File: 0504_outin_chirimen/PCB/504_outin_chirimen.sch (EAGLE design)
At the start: 34 parts

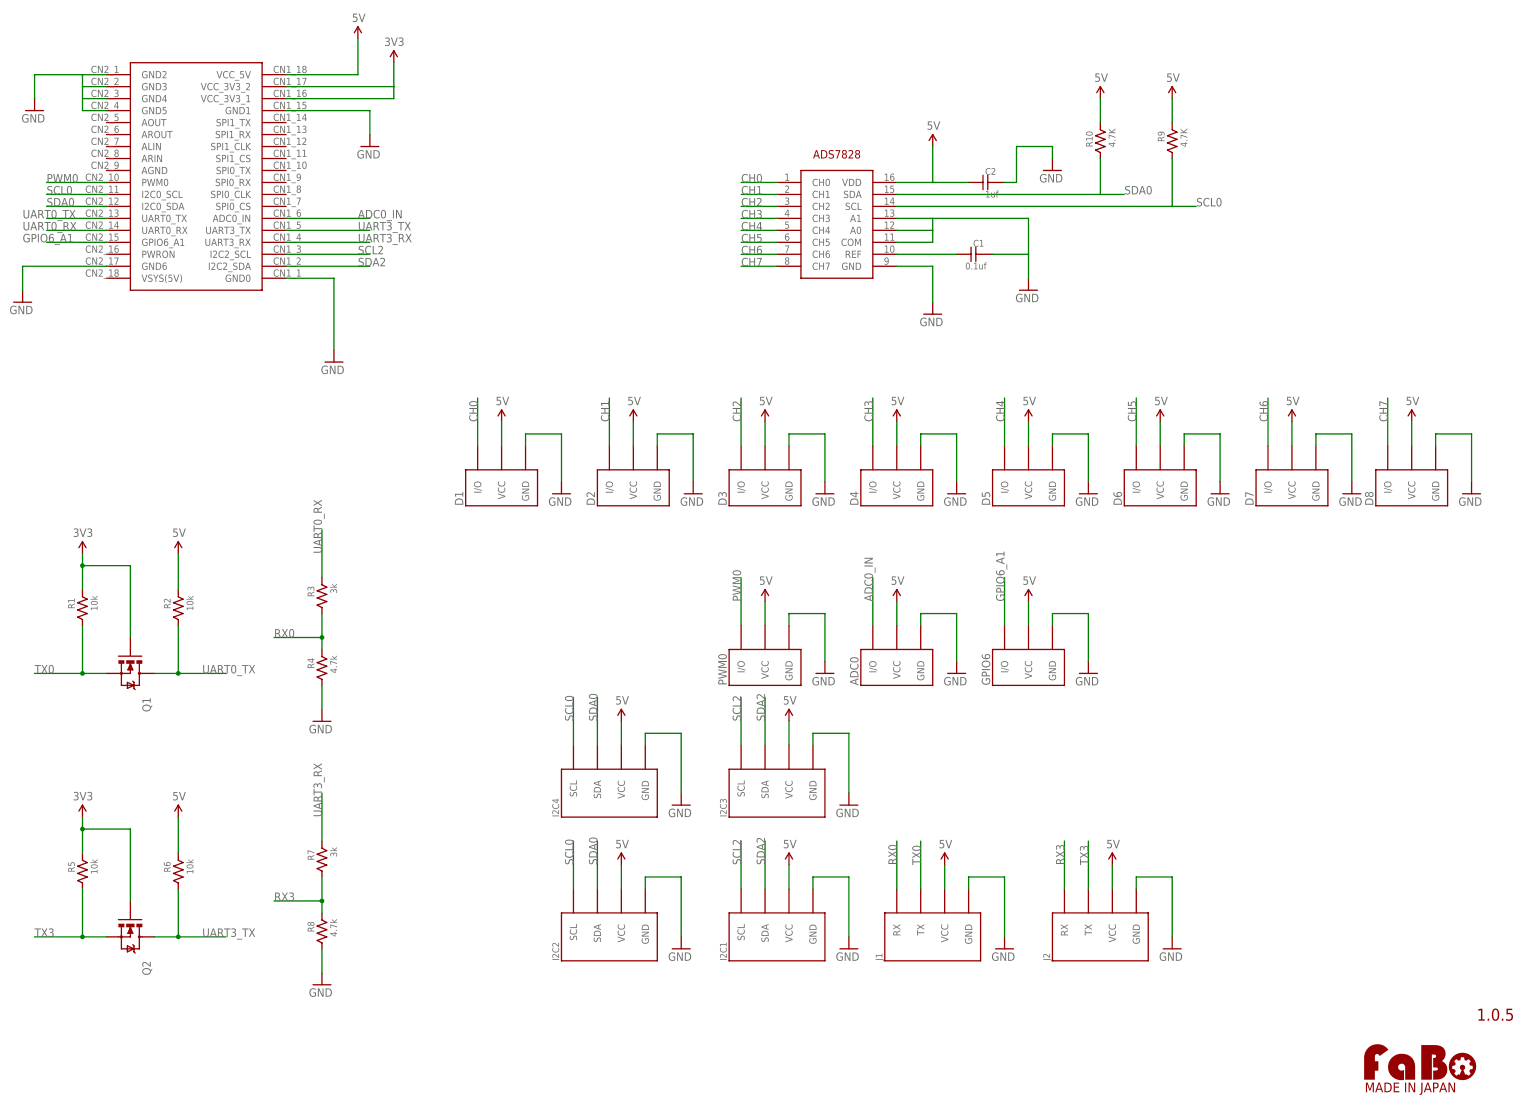
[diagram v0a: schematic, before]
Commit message: #504 outin_chirimen　ロゴ修正
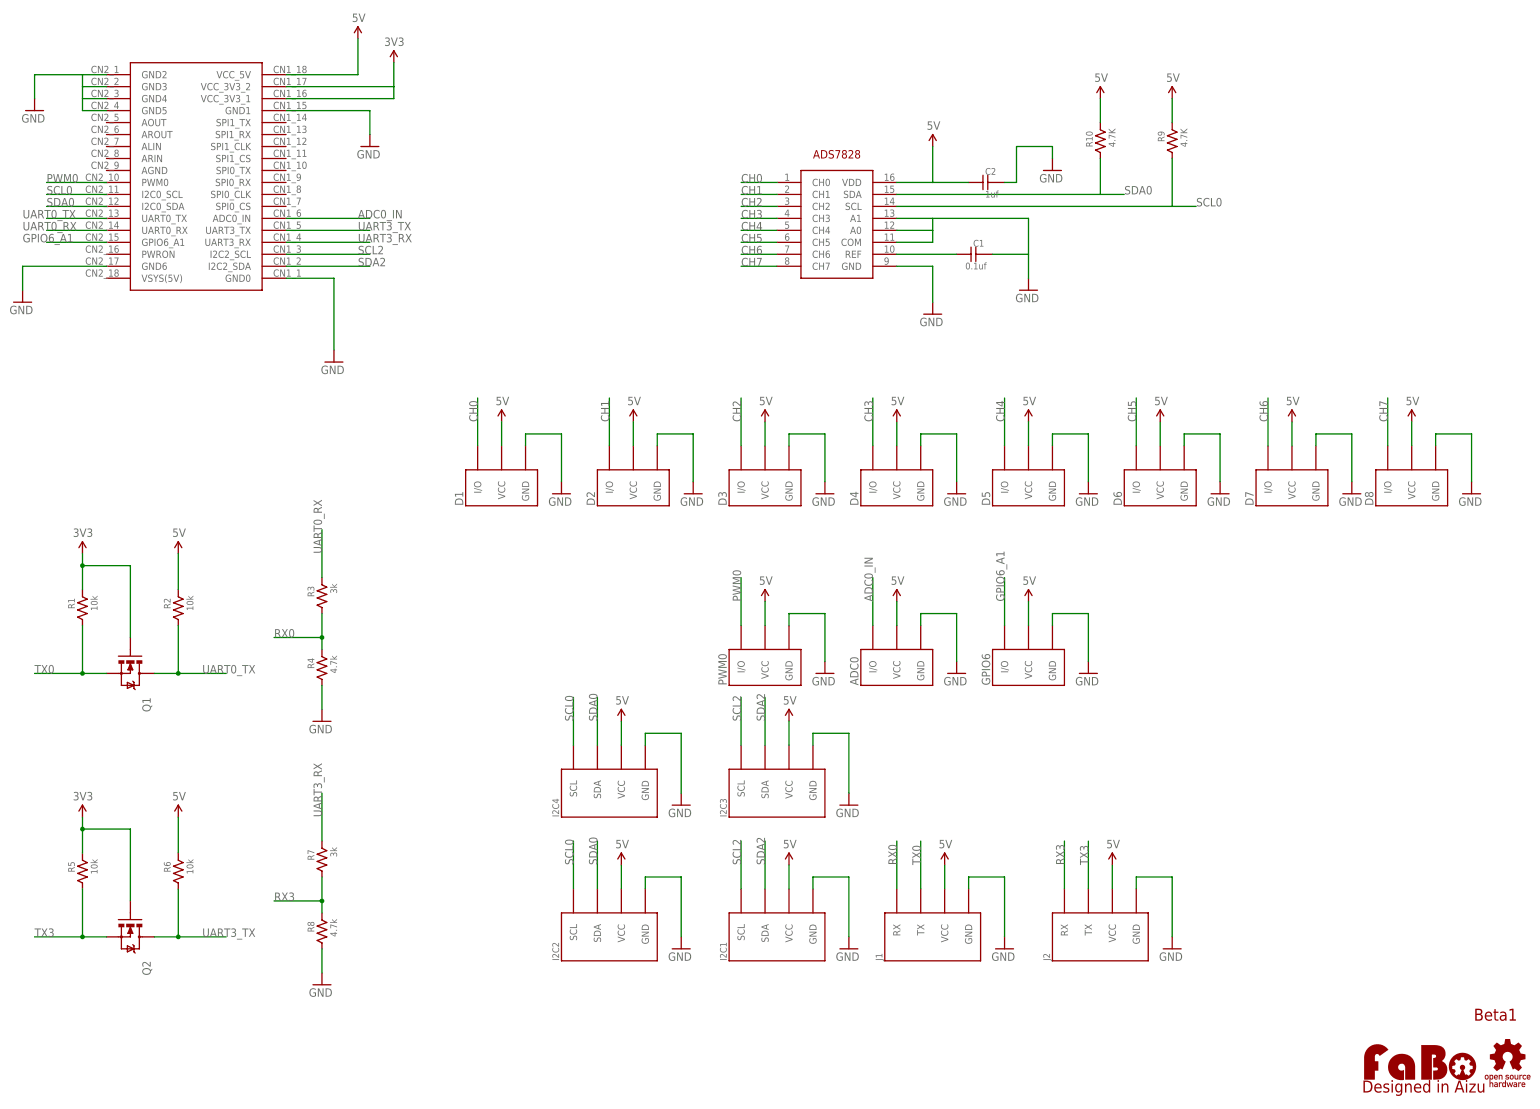
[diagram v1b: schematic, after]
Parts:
- removed U$10: (no value), FaBo-etc:LOGO_FABO-M
- added LOGO1: (no value), component:LOGO_FABO-M
- added U$3: LOGO_OSHW-M_BOTTOM, component:LOGO_OSHW-M_BOTTOM
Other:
- note added: "Beta1"
- note removed: "1.0.5"
